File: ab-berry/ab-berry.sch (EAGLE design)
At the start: 40 parts, among them U1 LM1117MPX-3.3/NOPB or AP2114H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

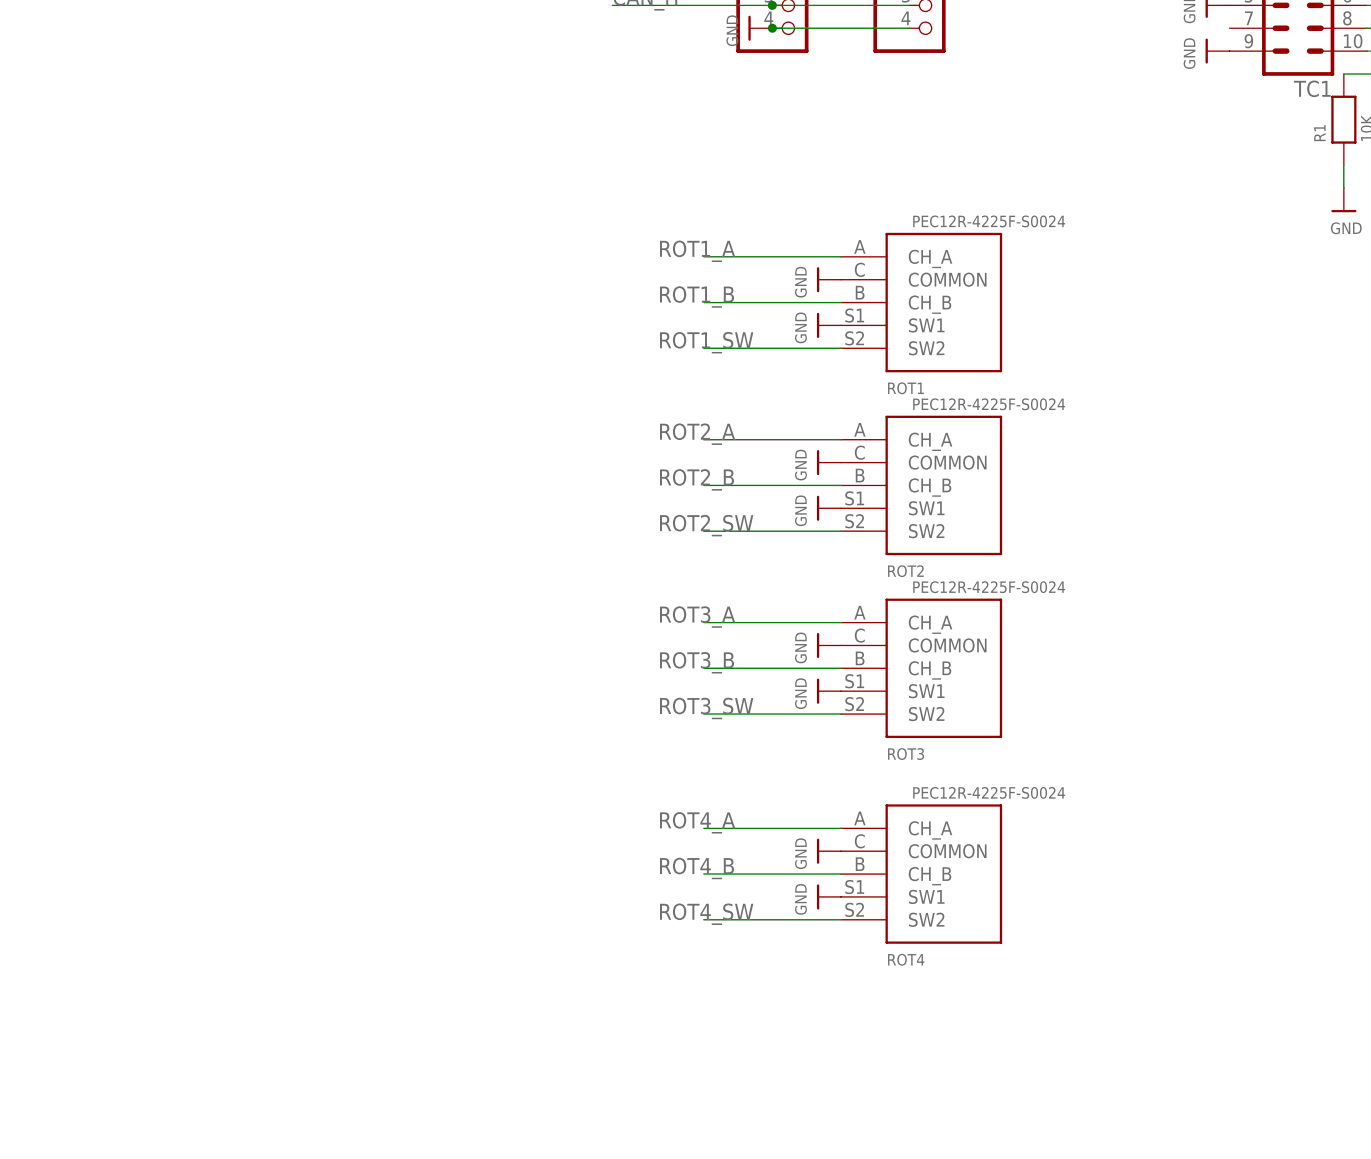
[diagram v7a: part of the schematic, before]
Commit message: ab-berry: add rc filter network to rotencs
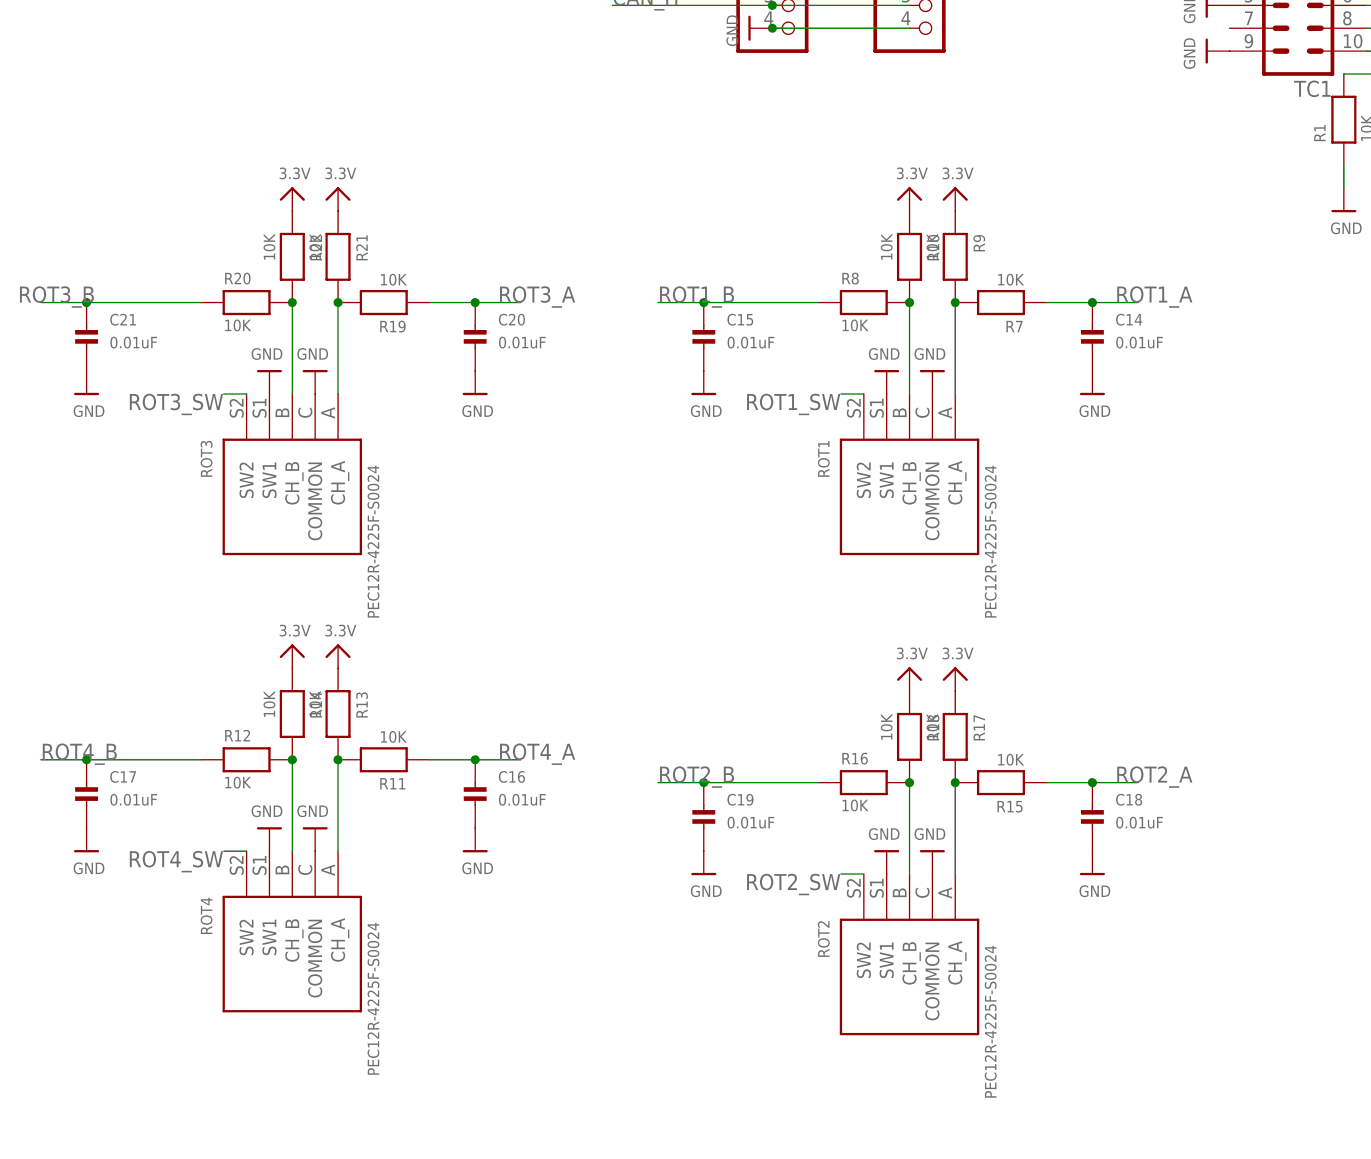
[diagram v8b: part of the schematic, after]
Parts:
- added C14, C15, C16, C17, C18, C19, C20, C21: 0.01uF, microbuilder:CAP_CERAMIC0603
- added R10, R11, R12, R13, R14, R15, R16, R17, R18, R19, R20, R21, R22, R7, R8, R9: 10K, microbuilder:RESISTOR0603
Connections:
- new net N$10: R10.2, R8.2, ROT1.CH_B
- new net N$11: R7.2, R9.2, ROT1.CH_A
- new net N$12: R12.2, R14.2, ROT4.CH_B
- new net N$13: R11.2, R13.2, ROT4.CH_A
- new net N$14: R16.2, R18.2, ROT2.CH_B
- new net N$15: R15.2, R17.2, ROT2.CH_A
- new net N$16: R20.2, R22.2, ROT3.CH_B
- new net N$17: R19.2, R21.2, ROT3.CH_A
- net 3.3V: now also R10.1, R13.1, R14.1, R17.1, R18.1, R21.1, R22.1, R9.1
- net GND: now also C14.P$2, C15.P$2, C16.P$2, C17.P$2, C18.P$2, C19.P$2, C20.P$2, C21.P$2
- net ROT1_A: now also C14.P$1, R7.1; no longer ROT1.CH_A
- net ROT1_B: now also C15.P$1, R8.1; no longer ROT1.CH_B
- net ROT2_A: now also C18.P$1, R15.1; no longer ROT2.CH_A
- net ROT2_B: now also C19.P$1, R16.1; no longer ROT2.CH_B
- net ROT3_A: now also C20.P$1, R19.1; no longer ROT3.CH_A
- net ROT3_B: now also C21.P$1, R20.1; no longer ROT3.CH_B
- net ROT4_A: now also C16.P$1, R11.1; no longer ROT4.CH_A
- net ROT4_B: now also C17.P$1, R12.1; no longer ROT4.CH_B
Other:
- moved on the sheet: ROT1, ROT2, ROT3, ROT4
